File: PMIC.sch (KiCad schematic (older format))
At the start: 20 parts, among them U4 STPMIC1APQR

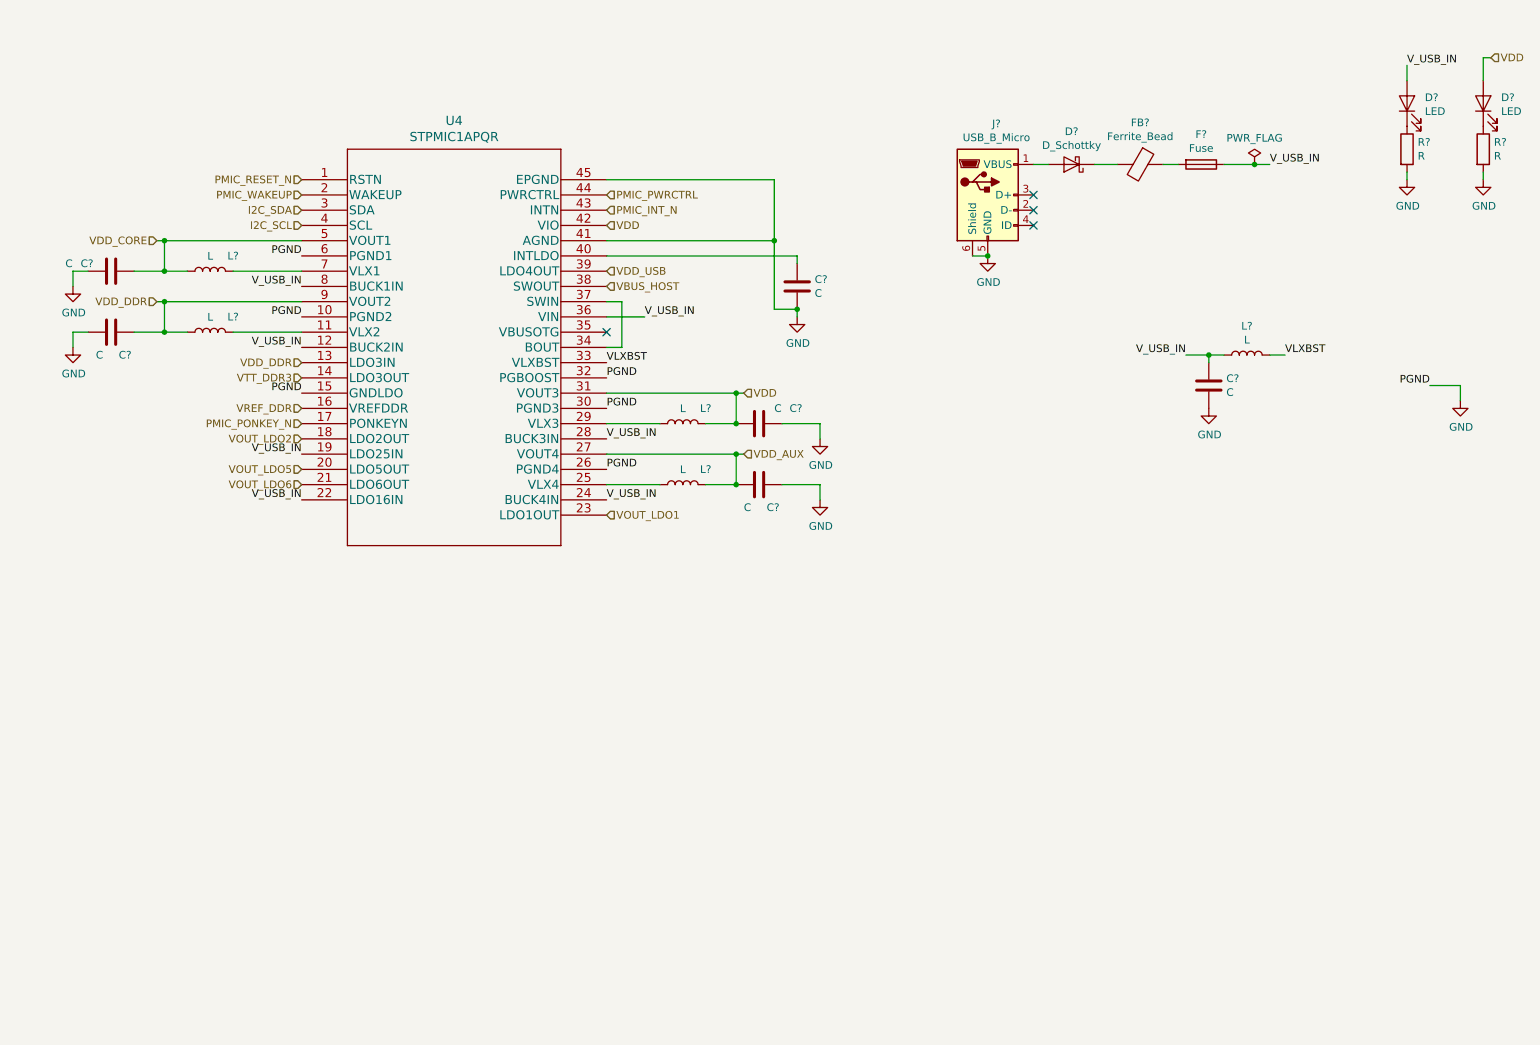
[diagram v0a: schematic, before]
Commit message: Add bulk labels for RAM and ethernet
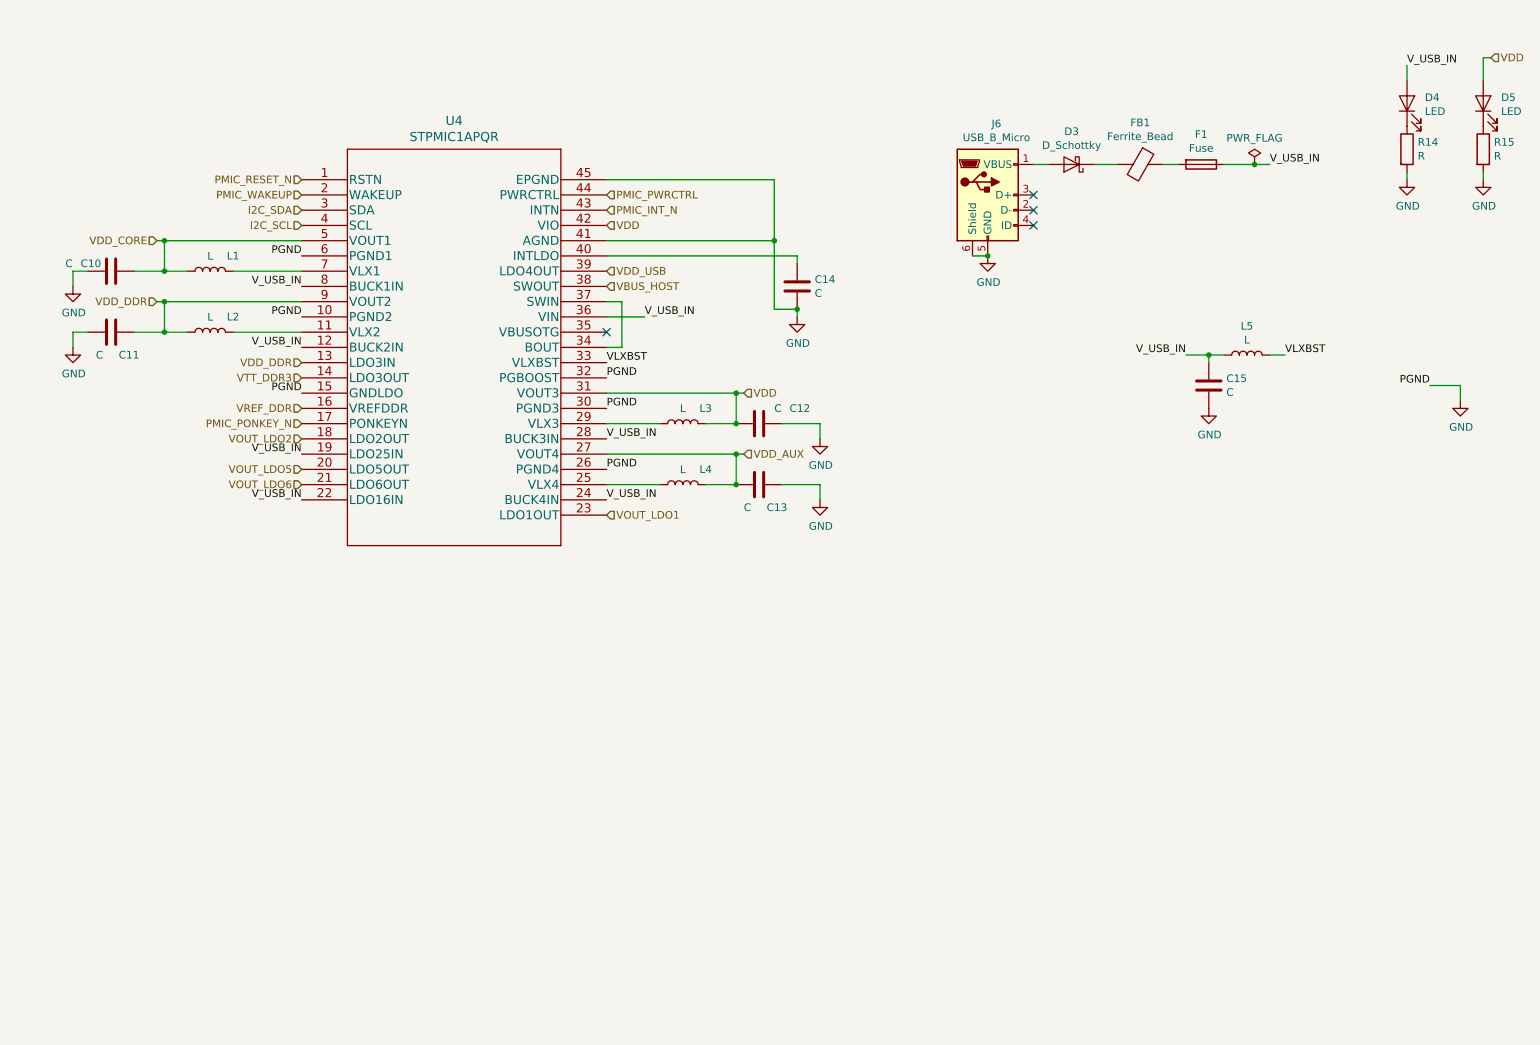
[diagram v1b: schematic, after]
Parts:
- C10, C11, C12, C13, C14, C15: renamed from C?; footprint (none) -> Capacitor_SMD:C_0603_1608Metric
- D3: renamed from D?; footprint (none) -> Diode_SMD:D_0603_1608Metric
- D4, D5: renamed from D?; footprint (none) -> LED_SMD:LED_0603_1608Metric
- F1: renamed from F?; footprint (none) -> Fuse:Fuse_0603_1608Metric
- FB1: renamed from FB?; footprint (none) -> Inductor_SMD:L_0603_1608Metric
- J6: renamed from J?; footprint (none) -> Connector_USB:USB_Micro-B_Amphenol_10103594-0001LF_Horizontal
- L1, L2, L3, L4, L5: renamed from L?; footprint (none) -> Inductor_SMD:L_0603_1608Metric
- R14, R15: renamed from R?; footprint (none) -> Resistor_SMD:R_0603_1608Metric
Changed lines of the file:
@@
 P 7500 1950
 AR Path="/601728C0/60637B7F" Ref="J?"  Part="1"
-AR Path="/60172B24/60637B7F" Ref="J?"  Part="1"
-F 0 "J?" H 7557 2417 50  0000 C CNN
+AR Path="/60172B24/60637B7F" Ref="J6"  Part="1"
+F 0 "J6" H 7557 2417 50  0000 C CNN
 F 1 "USB_B_Micro" H 7557 2326 50  0000 C CNN
-F 2 "" H 7650 1900 50  0001 C CNN
+F 2 "Connector_USB:USB_Micro-B_Amphenol_10103594-0001LF_Horizontal" H 7650 1900 50  0001 C CNN
 F 3 "~" H 7650 1900 50  0001 C CNN
 	1    7500 1950
@@
 P 8050 1750
 AR Path="/601728C0/60637B85" Ref="D?"  Part="1"
-AR Path="/60172B24/60637B85" Ref="D?"  Part="1"
-F 0 "D?" H 8050 1534 50  0000 C CNN
+AR Path="/60172B24/60637B85" Ref="D3"  Part="1"
+F 0 "D3" H 8050 1534 50  0000 C CNN
 F 1 "D_Schottky" H 8050 1625 50  0000 C CNN
-F 2 "" H 8050 1750 50  0001 C CNN
+F 2 "Diode_SMD:D_0603_1608Metric" H 8050 1750 50  0001 C CNN
 F 3 "~" H 8050 1750 50  0001 C CNN
 	1    8050 1750
@@
 P 8500 1750
 AR Path="/601728C0/60637B8B" Ref="FB?"  Part="1"
-AR Path="/60172B24/60637B8B" Ref="FB?"  Part="1"
-F 0 "FB?" V 8226 1750 50  0000 C CNN
+AR Path="/60172B24/60637B8B" Ref="FB1"  Part="1"
+F 0 "FB1" V 8226 1750 50  0000 C CNN
 F 1 "Ferrite_Bead" V 8317 1750 50  0000 C CNN
-F 2 "" V 8430 1750 50  0001 C CNN
+F 2 "Inductor_SMD:L_0603_1608Metric" V 8430 1750 50  0001 C CNN
 F 3 "~" H 8500 1750 50  0001 C CNN
 	1    8500 1750
@@
 P 8900 1750
 AR Path="/601728C0/60637B91" Ref="F?"  Part="1"
-AR Path="/60172B24/60637B91" Ref="F?"  Part="1"
-F 0 "F?" V 8703 1750 50  0000 C CNN
+AR Path="/60172B24/60637B91" Ref="F1"  Part="1"
+F 0 "F1" V 8703 1750 50  0000 C CNN
 F 1 "Fuse" V 8794 1750 50  0000 C CNN
-F 2 "" V 8830 1750 50  0001 C CNN
+F 2 "Fuse:Fuse_0603_1608Metric" V 8830 1750 50  0001 C CNN
 F 3 "~" H 8900 1750 50  0001 C CNN
 	1    8900 1750
@@
 P 7500 2350
 AR Path="/601728C0/60637B9E" Ref="#PWR?"  Part="1"
-AR Path="/60172B24/60637B9E" Ref="#PWR?"  Part="1"
-F 0 "#PWR?" H 7500 2100 50  0001 C CNN
+AR Path="/60172B24/60637B9E" Ref="#PWR026"  Part="1"
+F 0 "#PWR026" H 7500 2100 50  0001 C CNN
 F 1 "GND" H 7505 2177 50  0000 C CNN
 F 2 "" H 7500 2350 50  0001 C CNN
@@
 P 9250 1750
 AR Path="/601728C0/60637BA5" Ref="#FLG?"  Part="1"
-AR Path="/60172B24/60637BA5" Ref="#FLG?"  Part="1"
-F 0 "#FLG?" H 9250 1825 50  0001 C CNN
+AR Path="/60172B24/60637BA5" Ref="#FLG01"  Part="1"
+F 0 "#FLG01" H 9250 1825 50  0001 C CNN
 F 1 "PWR_FLAG" H 9250 1923 50  0000 C CNN
 F 2 "" H 9250 1750 50  0001 C CNN
@@
 V_USB_IN
 $Comp
-L Device:R R?
+L Device:R R14
 U 1 1 6063A1CC
 P 10250 1650
-F 0 "R?" H 10320 1696 50  0000 L CNN
+F 0 "R14" H 10320 1696 50  0000 L CNN
 F 1 "R" H 10320 1605 50  0000 L CNN
-F 2 "" V 10180 1650 50  0001 C CNN
+F 2 "Resistor_SMD:R_0603_1608Metric" V 10180 1650 50  0001 C CNN
 F 3 "~" H 10250 1650 50  0001 C CNN
 	1    10250 1650
@@
 $EndComp
 $Comp
-L Device:LED D?
+L Device:LED D4
 U 1 1 6063A7AA
 P 10250 1350
-F 0 "D?" V 10289 1233 50  0000 R CNN
+F 0 "D4" V 10289 1233 50  0000 R CNN
 F 1 "LED" V 10198 1233 50  0000 R CNN
-F 2 "" H 10250 1350 50  0001 C CNN
+F 2 "LED_SMD:LED_0603_1608Metric" H 10250 1350 50  0001 C CNN
 F 3 "~" H 10250 1350 50  0001 C CNN
 	1    10250 1350
@@
 	10250 1100 10250 1200
 $Comp
-L power:GND #PWR?
+L power:GND #PWR028
 U 1 1 6063B1C3
 P 10250 1850
-F 0 "#PWR?" H 10250 1600 50  0001 C CNN
+F 0 "#PWR028" H 10250 1600 50  0001 C CNN
 F 1 "GND" H 10255 1677 50  0000 C CNN
 F 2 "" H 10250 1850 50  0001 C CNN
@@
 I2C_SCL
 $Comp
-L Device:L L?
+L Device:L L1
 U 1 1 60EF8DCB
 P 2400 2450
-F 0 "L?" V 2500 2300 50  0000 C CNN
+F 0 "L1" V 2500 2300 50  0000 C CNN
 F 1 "L" V 2499 2450 50  0000 C CNN
-F 2 "" H 2400 2450 50  0001 C CNN
+F 2 "Inductor_SMD:L_0603_1608Metric" H 2400 2450 50  0001 C CNN
 F 3 "~" H 2400 2450 50  0001 C CNN
 	1    2400 2450
@@
 $EndComp
 $Comp
-L Device:C C?
+L Device:C C10
 U 1 1 60EF9810
 P 1750 2450
-F 0 "C?" V 1700 2250 50  0000 L CNN
+F 0 "C10" V 1700 2250 50  0000 L CNN
 F 1 "C" V 1700 2150 50  0000 L CNN
-F 2 "" H 1788 2300 50  0001 C CNN
+F 2 "Capacitor_SMD:C_0603_1608Metric" H 1788 2300 50  0001 C CNN
 F 3 "~" H 1750 2450 50  0001 C CNN
 	1    1750 2450
@@
 	2100 2250 3000 2250
 $Comp
-L Device:L L?
+L Device:L L2
 U 1 1 60F03A6C
 P 2400 2850
-F 0 "L?" V 2500 2700 50  0000 C CNN
+F 0 "L2" V 2500 2700 50  0000 C CNN
 F 1 "L" V 2499 2850 50  0000 C CNN
-F 2 "" H 2400 2850 50  0001 C CNN
+F 2 "Inductor_SMD:L_0603_1608Metric" H 2400 2850 50  0001 C CNN
 F 3 "~" H 2400 2850 50  0001 C CNN
 	1    2400 2850
@@
 $EndComp
 $Comp
-L Device:C C?
+L Device:C C11
 U 1 1 60F03A72
 P 1750 2850
-F 0 "C?" V 1900 2900 50  0000 L CNN
+F 0 "C11" V 1900 2900 50  0000 L CNN
 F 1 "C" V 1900 2750 50  0000 L CNN
-F 2 "" H 1788 2700 50  0001 C CNN
+F 2 "Capacitor_SMD:C_0603_1608Metric" H 1788 2700 50  0001 C CNN
 F 3 "~" H 1750 2850 50  0001 C CNN
 	1    1750 2850
@@
 	2550 2850 3000 2850
 $Comp
-L power:GND #PWR?
+L power:GND #PWR022
 U 1 1 60F0CC5C
 P 1500 2950
-F 0 "#PWR?" H 1500 2700 50  0001 C CNN
+F 0 "#PWR022" H 1500 2700 50  0001 C CNN
 F 1 "GND" H 1505 2777 50  0000 C CNN
 F 2 "" H 1500 2950 50  0001 C CNN
@@
 	1500 2850 1600 2850
 $Comp
-L power:GND #PWR?
+L power:GND #PWR021
 U 1 1 60F0E51B
 P 1500 2550
-F 0 "#PWR?" H 1500 2300 50  0001 C CNN
+F 0 "#PWR021" H 1500 2300 50  0001 C CNN
 F 1 "GND" H 1505 2377 50  0000 C CNN
 F 2 "" H 1500 2550 50  0001 C CNN
@@
 	1500 2450 1600 2450
 $Comp
-L Device:L L?
+L Device:L L3
 U 1 1 60F16310
 P 5500 3450
-F 0 "L?" V 5600 3300 50  0000 C CNN
+F 0 "L3" V 5600 3300 50  0000 C CNN
 F 1 "L" V 5599 3450 50  0000 C CNN
-F 2 "" H 5500 3450 50  0001 C CNN
+F 2 "Inductor_SMD:L_0603_1608Metric" H 5500 3450 50  0001 C CNN
 F 3 "~" H 5500 3450 50  0001 C CNN
 	1    5500 3450
@@
 $EndComp
 $Comp
-L Device:C C?
+L Device:C C12
 U 1 1 60F16316
 P 6000 3450
-F 0 "C?" V 5900 3650 50  0000 L CNN
+F 0 "C12" V 5900 3650 50  0000 L CNN
 F 1 "C" V 5900 3550 50  0000 L CNN
-F 2 "" H 6038 3300 50  0001 C CNN
+F 2 "Capacitor_SMD:C_0603_1608Metric" H 6038 3300 50  0001 C CNN
 F 3 "~" H 6000 3450 50  0001 C CNN
 	1    6000 3450
@@
 $EndComp
 $Comp
-L power:GND #PWR?
+L power:GND #PWR024
 U 1 1 60F1631F
 P 6400 3550
-F 0 "#PWR?" H 6400 3300 50  0001 C CNN
+F 0 "#PWR024" H 6400 3300 50  0001 C CNN
 F 1 "GND" H 6405 3377 50  0000 C CNN
 F 2 "" H 6400 3550 50  0001 C CNN
@@
 Connection ~ 5850 3450
 $Comp
-L Device:L L?
+L Device:L L4
 U 1 1 60F2C5C2
 P 5500 3850
-F 0 "L?" V 5600 3700 50  0000 C CNN
+F 0 "L4" V 5600 3700 50  0000 C CNN
 F 1 "L" V 5599 3850 50  0000 C CNN
-F 2 "" H 5500 3850 50  0001 C CNN
+F 2 "Inductor_SMD:L_0603_1608Metric" H 5500 3850 50  0001 C CNN
 F 3 "~" H 5500 3850 50  0001 C CNN
 	1    5500 3850
@@
 $EndComp
 $Comp
-L Device:C C?
+L Device:C C13
 U 1 1 60F2C5C8
 P 6000 3850
-F 0 "C?" V 6150 3900 50  0000 L CNN
+F 0 "C13" V 6150 3900 50  0000 L CNN
 F 1 "C" V 6150 3750 50  0000 L CNN
-F 2 "" H 6038 3700 50  0001 C CNN
+F 2 "Capacitor_SMD:C_0603_1608Metric" H 6038 3700 50  0001 C CNN
 F 3 "~" H 6000 3850 50  0001 C CNN
 	1    6000 3850
@@
 $EndComp
 $Comp
-L power:GND #PWR?
+L power:GND #PWR025
 U 1 1 60F2C5CE
 P 6400 3950
-F 0 "#PWR?" H 6400 3700 50  0001 C CNN
+F 0 "#PWR025" H 6400 3700 50  0001 C CNN
 F 1 "GND" H 6405 3777 50  0000 C CNN
 F 2 "" H 6400 3950 50  0001 C CNN
@@
 VDD_DDR
 $Comp
-L Device:L L?
+L Device:L L5
 U 1 1 60F7B71F
 P 9200 3000
-F 0 "L?" V 9390 3000 50  0000 C CNN
+F 0 "L5" V 9390 3000 50  0000 C CNN
 F 1 "L" V 9299 3000 50  0000 C CNN
-F 2 "" H 9200 3000 50  0001 C CNN
+F 2 "Inductor_SMD:L_0603_1608Metric" H 9200 3000 50  0001 C CNN
 F 3 "~" H 9200 3000 50  0001 C CNN
 	1    9200 3000
@@
 VLXBST
 $Comp
-L Device:C C?
+L Device:C C15
 U 1 1 60F93081
 P 8950 3200
-F 0 "C?" H 9065 3246 50  0000 L CNN
+F 0 "C15" H 9065 3246 50  0000 L CNN
 F 1 "C" H 9065 3155 50  0000 L CNN
-F 2 "" H 8988 3050 50  0001 C CNN
+F 2 "Capacitor_SMD:C_0603_1608Metric" H 8988 3050 50  0001 C CNN
 F 3 "~" H 8950 3200 50  0001 C CNN
 	1    8950 3200
@@
 V_USB_IN
 $Comp
-L power:GND #PWR?
+L power:GND #PWR027
 U 1 1 60FA0DFB
 P 8950 3350
-F 0 "#PWR?" H 8950 3100 50  0001 C CNN
+F 0 "#PWR027" H 8950 3100 50  0001 C CNN
 F 1 "GND" H 8955 3177 50  0000 C CNN
 F 2 "" H 8950 3350 50  0001 C CNN
@@
 	5000 2350 6250 2350
 $Comp
-L Device:C C?
+L Device:C C14
 U 1 1 60FAFC3A
 P 6250 2550
-F 0 "C?" H 6365 2596 50  0000 L CNN
+F 0 "C14" H 6365 2596 50  0000 L CNN
 F 1 "C" H 6365 2505 50  0000 L CNN
-F 2 "" H 6288 2400 50  0001 C CNN
+F 2 "Capacitor_SMD:C_0603_1608Metric" H 6288 2400 50  0001 C CNN
 F 3 "~" H 6250 2550 50  0001 C CNN
 	1    6250 2550
@@
 $EndComp
 $Comp
-L power:GND #PWR?
+L power:GND #PWR023
 U 1 1 60FB16CE
 P 6250 2750
-F 0 "#PWR?" H 6250 2500 50  0001 C CNN
+F 0 "#PWR023" H 6250 2500 50  0001 C CNN
 F 1 "GND" H 6255 2577 50  0000 C CNN
 F 2 "" H 6250 2750 50  0001 C CNN
@@
 	10600 3200 10600 3300
 $Comp
-L power:GND #PWR?
+L power:GND #PWR029
 U 1 1 60FFDCB0
 P 10600 3300
-F 0 "#PWR?" H 10600 3050 50  0001 C CNN
+F 0 "#PWR029" H 10600 3050 50  0001 C CNN
 F 1 "GND" H 10605 3127 50  0000 C CNN
 F 2 "" H 10600 3300 50  0001 C CNN
@@
 $EndComp
 $Comp
-L Device:R R?
+L Device:R R15
 U 1 1 61003C3B
 P 10750 1650
-F 0 "R?" H 10820 1696 50  0000 L CNN
+F 0 "R15" H 10820 1696 50  0000 L CNN
 F 1 "R" H 10820 1605 50  0000 L CNN
-F 2 "" V 10680 1650 50  0001 C CNN
+F 2 "Resistor_SMD:R_0603_1608Metric" V 10680 1650 50  0001 C CNN
 F 3 "~" H 10750 1650 50  0001 C CNN
 	1    10750 1650
@@
 $EndComp
 $Comp
-L Device:LED D?
+L Device:LED D5
 U 1 1 61003C41
 P 10750 1350
-F 0 "D?" V 10789 1233 50  0000 R CNN
+F 0 "D5" V 10789 1233 50  0000 R CNN
 F 1 "LED" V 10698 1233 50  0000 R CNN
-F 2 "" H 10750 1350 50  0001 C CNN
+F 2 "LED_SMD:LED_0603_1608Metric" H 10750 1350 50  0001 C CNN
 F 3 "~" H 10750 1350 50  0001 C CNN
 	1    10750 1350
@@
 $EndComp
 $Comp
-L power:GND #PWR?
+L power:GND #PWR030
 U 1 1 61003C47
 P 10750 1850
-F 0 "#PWR?" H 10750 1600 50  0001 C CNN
+F 0 "#PWR030" H 10750 1600 50  0001 C CNN
 F 1 "GND" H 10755 1677 50  0000 C CNN
 F 2 "" H 10750 1850 50  0001 C CNN

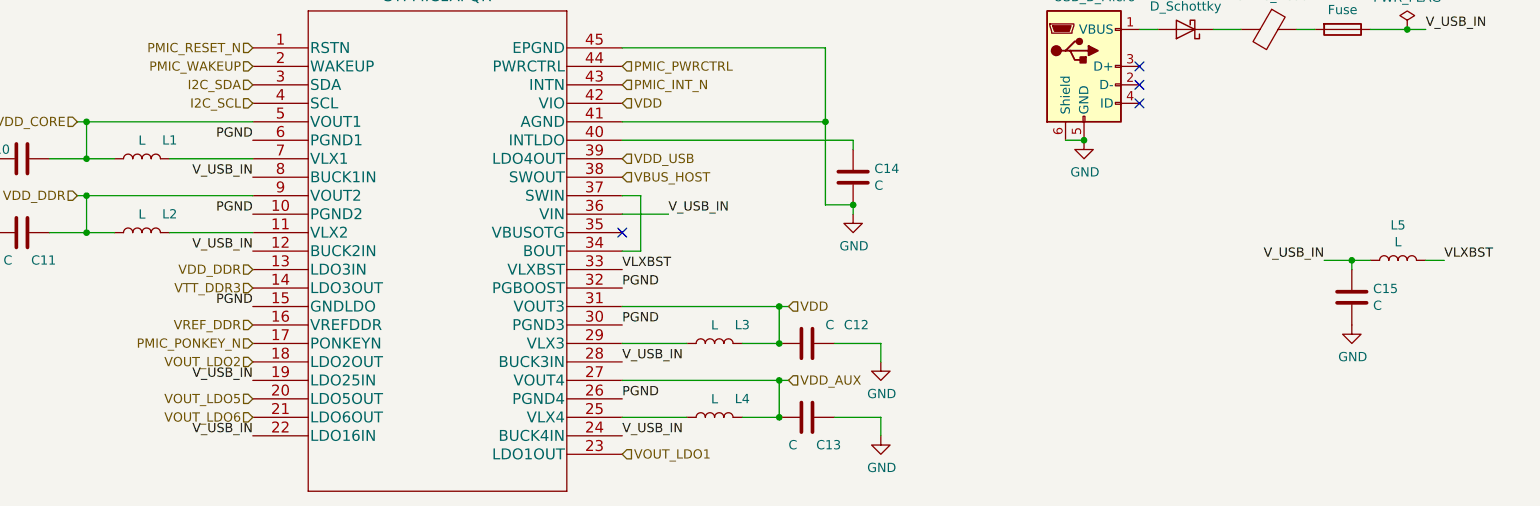
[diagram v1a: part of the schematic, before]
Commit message: Add decoupling capacitors
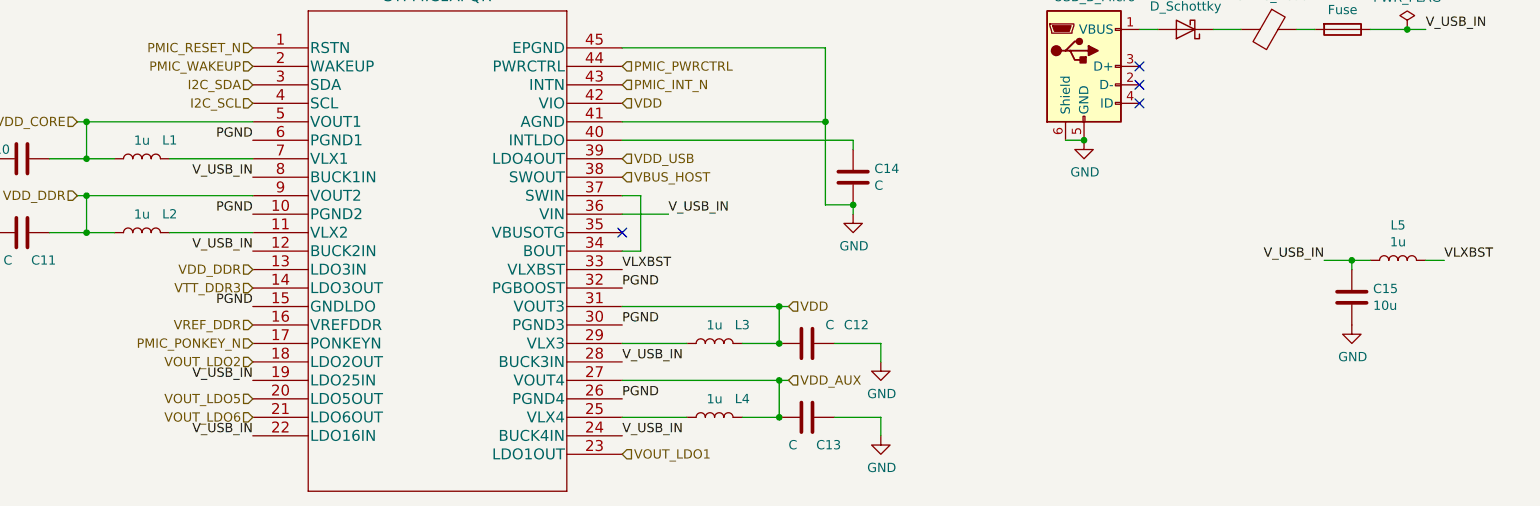
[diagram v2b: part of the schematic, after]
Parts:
- C15: value C -> 10u
- L1, L2, L3, L4, L5: value L -> 1u
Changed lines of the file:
@@
 P 2400 2450
 F 0 "L1" V 2500 2300 50  0000 C CNN
-F 1 "L" V 2499 2450 50  0000 C CNN
+F 1 "1u" V 2499 2450 50  0000 C CNN
 F 2 "Inductor_SMD:L_0603_1608Metric" H 2400 2450 50  0001 C CNN
 F 3 "~" H 2400 2450 50  0001 C CNN
@@
 P 2400 2850
 F 0 "L2" V 2500 2700 50  0000 C CNN
-F 1 "L" V 2499 2850 50  0000 C CNN
+F 1 "1u" V 2499 2850 50  0000 C CNN
 F 2 "Inductor_SMD:L_0603_1608Metric" H 2400 2850 50  0001 C CNN
 F 3 "~" H 2400 2850 50  0001 C CNN
@@
 P 5500 3450
 F 0 "L3" V 5600 3300 50  0000 C CNN
-F 1 "L" V 5599 3450 50  0000 C CNN
+F 1 "1u" V 5599 3450 50  0000 C CNN
 F 2 "Inductor_SMD:L_0603_1608Metric" H 5500 3450 50  0001 C CNN
 F 3 "~" H 5500 3450 50  0001 C CNN
@@
 P 5500 3850
 F 0 "L4" V 5600 3700 50  0000 C CNN
-F 1 "L" V 5599 3850 50  0000 C CNN
+F 1 "1u" V 5599 3850 50  0000 C CNN
 F 2 "Inductor_SMD:L_0603_1608Metric" H 5500 3850 50  0001 C CNN
 F 3 "~" H 5500 3850 50  0001 C CNN
@@
 P 9200 3000
 F 0 "L5" V 9390 3000 50  0000 C CNN
-F 1 "L" V 9299 3000 50  0000 C CNN
+F 1 "1u" V 9299 3000 50  0000 C CNN
 F 2 "Inductor_SMD:L_0603_1608Metric" H 9200 3000 50  0001 C CNN
 F 3 "~" H 9200 3000 50  0001 C CNN
@@
 P 8950 3200
 F 0 "C15" H 9065 3246 50  0000 L CNN
-F 1 "C" H 9065 3155 50  0000 L CNN
+F 1 "10u" H 9065 3155 50  0000 L CNN
 F 2 "Capacitor_SMD:C_0603_1608Metric" H 8988 3050 50  0001 C CNN
 F 3 "~" H 8950 3200 50  0001 C CNN
